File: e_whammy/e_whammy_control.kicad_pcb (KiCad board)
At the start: 2 copper layers, 32 x 10 mm, 29 parts, among them J1 Conn_01x03, J2 Conn_01x03, U1 MCP1501T-25E/CHY, U2 HT7550-1, U3 TLV9002IDGKR, U4 ADG779, U5 LM393BIDGKR

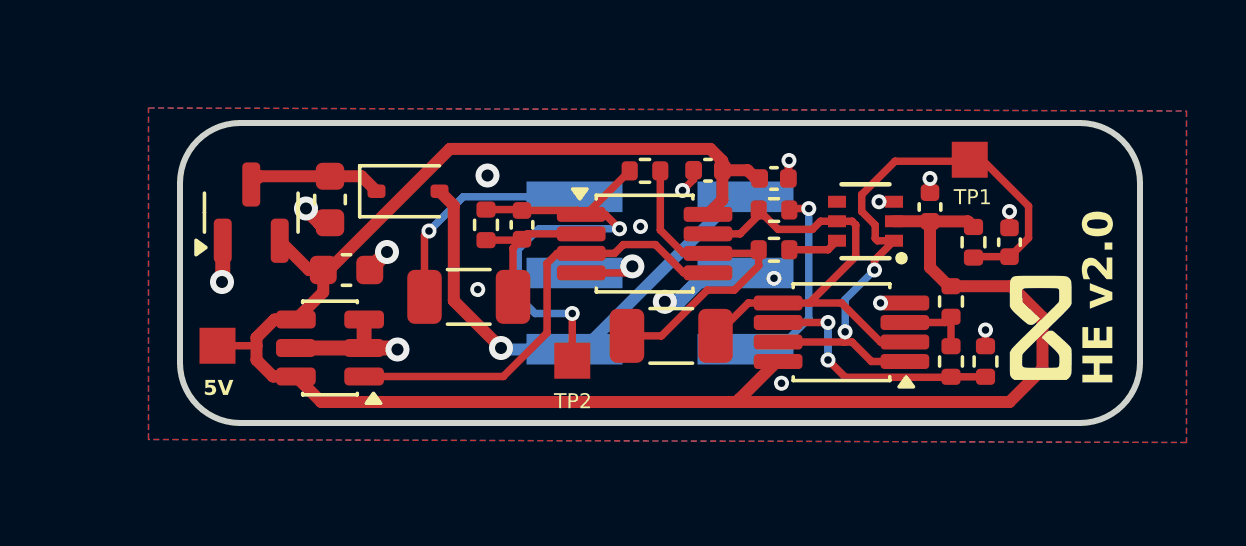
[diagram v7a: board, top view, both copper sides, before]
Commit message: Change voltage reference to a more common type TI REF3025AIDBZR
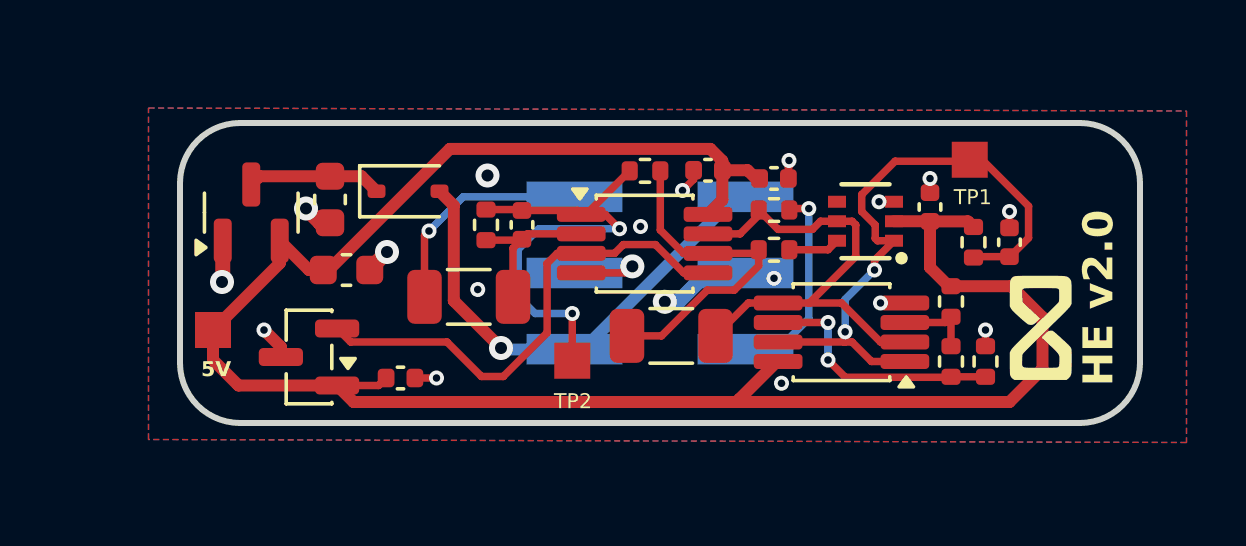
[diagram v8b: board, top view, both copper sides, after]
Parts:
- removed U1: MCP1501T-25E/CHY, Package_TO_SOT_SMD:SOT-23-6
- added C10: 100nF, Capacitor_SMD:C_0402_1005Metric, F.Cu at (146.2, 149.5)
- added U6: REF3025, Package_TO_SOT_SMD:SOT-23, F.Cu at (143.2, 148.8)
- U4: value ADG779 -> TPADG779BKSZ
- moved TP3 0.55 mm to (140.0, 147.9)
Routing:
- net GND: track 16.8 -> 14.3 mm, vias 18 -> 19
- net 5v: track 65.5 -> 68.0 mm
- net VREF: track 15.0 -> 16.6 mm
